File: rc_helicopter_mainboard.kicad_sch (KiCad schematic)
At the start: 15 parts, among them J1 Conn_01x06, SW1 Tactswitch, U1 STM32L4P5RET6, Y1 16MHz

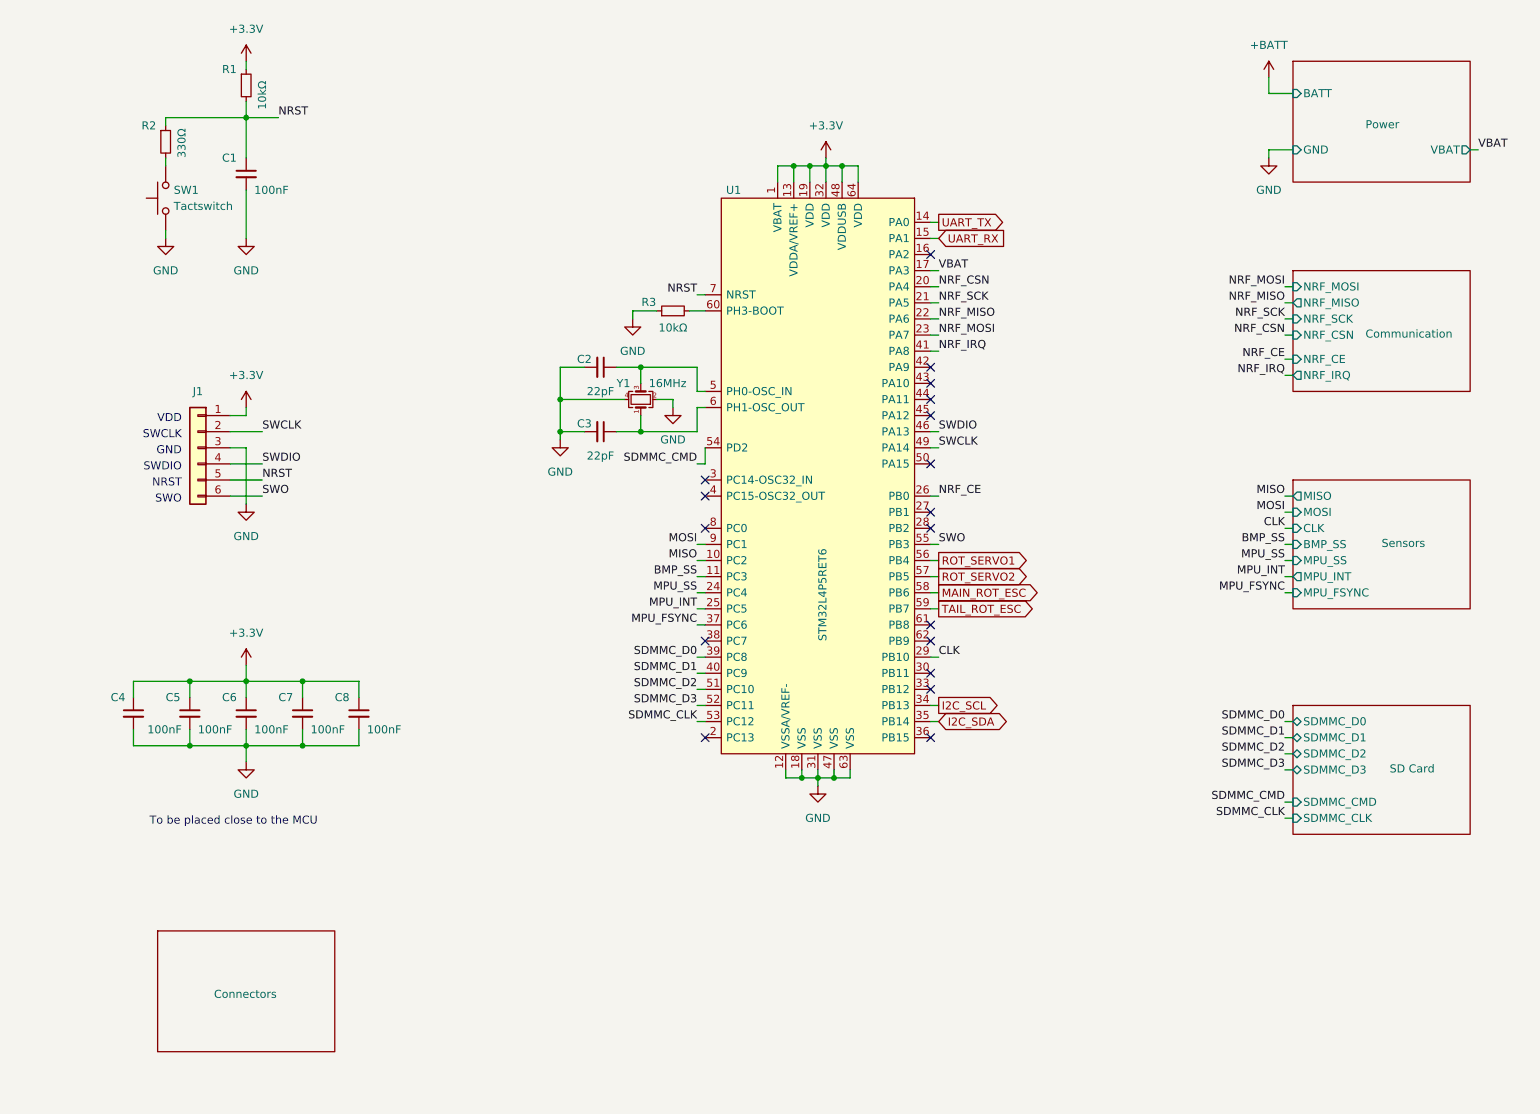
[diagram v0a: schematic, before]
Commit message: Use single connector for I/O
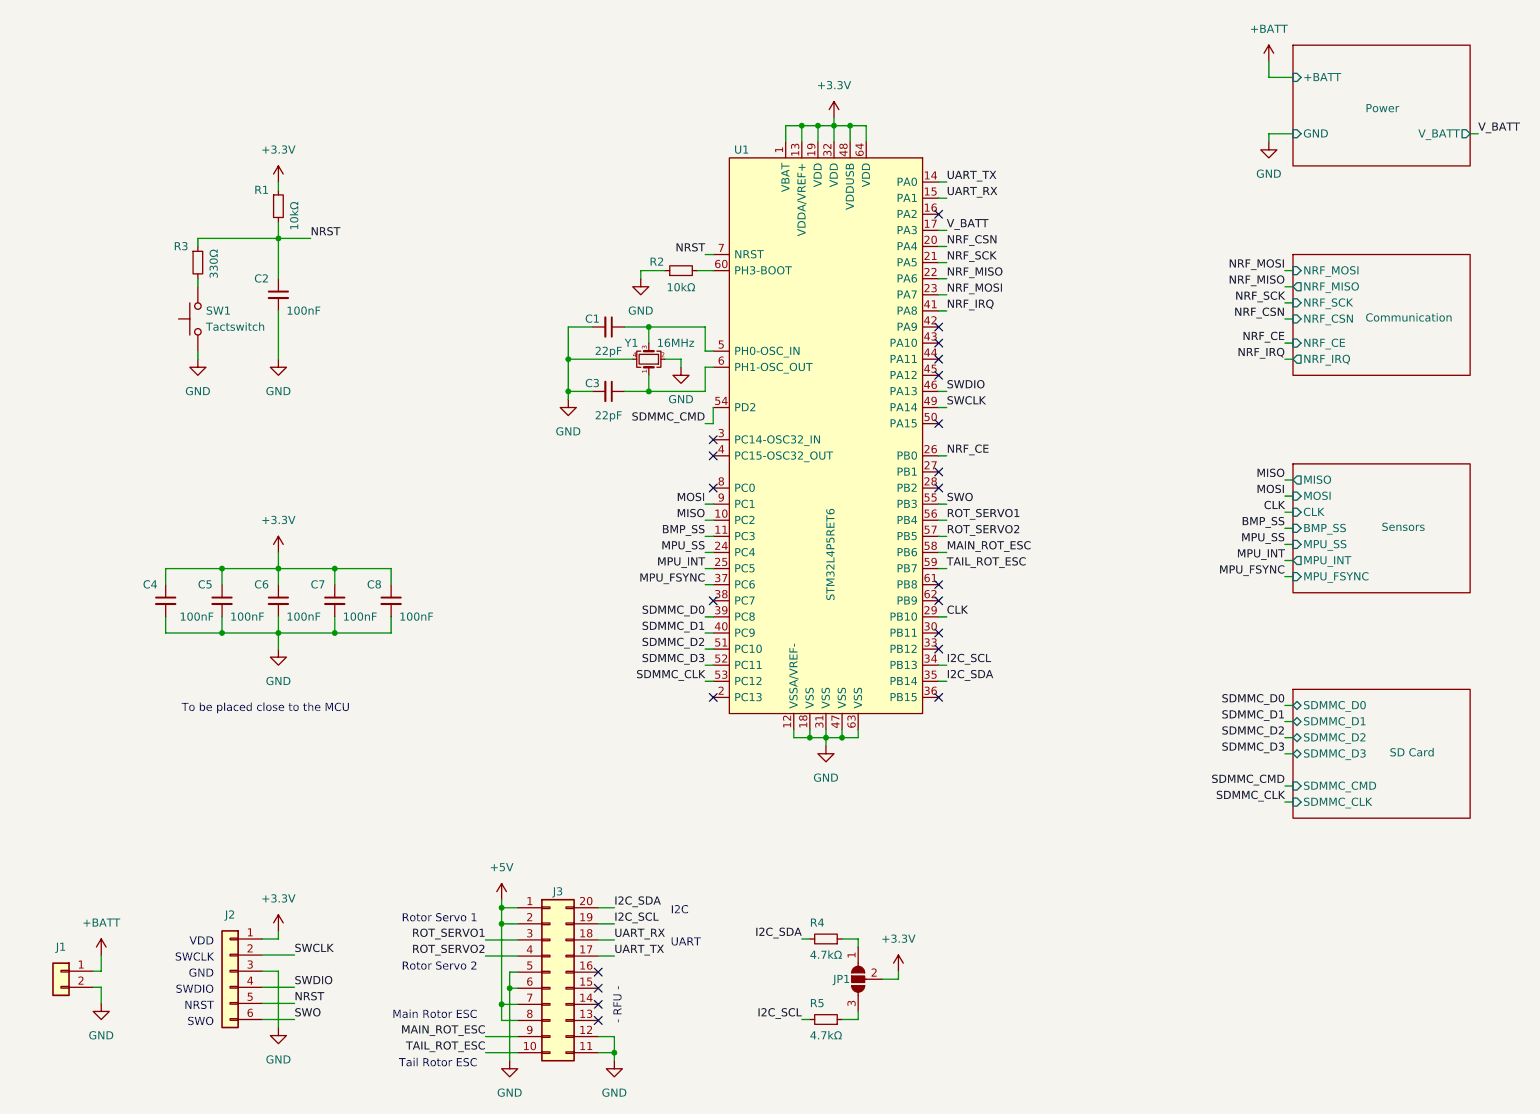
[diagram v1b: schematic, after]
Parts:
- added J1: Battery Pack, Connector_Molex:Molex_KK-254_AE-6410-02A_1x02_P2.54mm_Vertical, symbol Connector_Generic:Conn_01x02
- added J3: Main Connector, Connector_PinHeader_2.54mm:PinHeader_2x10_P2.54mm_Horizontal, symbol Connector_Generic:Conn_02x10_Counter_Clockwise
- added JP1: SolderJumper_3_Open, Jumper:SolderJumper-3_P1.3mm_Open_RoundedPad1.0x1.5mm_NumberLabels, symbol Jumper:SolderJumper_3_Open
- added R4, R5: 4.7kΩ, Resistor_SMD:R_0603_1608Metric, symbol Device:R_Small
- J2: renamed from J1; value Conn_01x06 -> SWD; footprint Connector_PinHeader_2.54mm:PinHeader_1x06_P2.54mm_Vertical_SMD_Pin1Left -> Connector_PinHeader_2.54mm:PinHeader_2x03_P2.54mm_Vertical
- renumbered C2 to C1, C1 to C2, R3 to R2, R2 to R3
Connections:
- net +3.3V: now also JP1.2 (C)
- net +BATT: now also J1.1 (Pin_1)
- net GND: now also J1.2 (Pin_2), J3.11 (Pin_11), J3.12 (Pin_12), J3.5 (Pin_5), J3.6 (Pin_6)
- net I2C_SCL: now also J3.19 (Pin_19), R5.2
- net I2C_SDA: now also J3.20 (Pin_20), R4.2
- net MAIN_ROT_ESC: now also J3.9 (Pin_9)
- net ROT_SERVO1: now also J3.3 (Pin_3)
- net ROT_SERVO2: now also J3.4 (Pin_4)
- net TAIL_ROT_ESC: now also J3.10 (Pin_10)
- net UART_RX: now also J3.18 (Pin_18)
- net UART_TX: now also J3.17 (Pin_17)
- net VBAT renamed V_BATT
- new net: JP1.1 (A), R4.1
- new net: JP1.3 (B), R5.1
- new net +5V: J3.1 (Pin_1), J3.2 (Pin_2), J3.7 (Pin_7), J3.8 (Pin_8)
- no-connect marks 18 -> 22
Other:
- removed sheet Connectors
- sheet Power ports: added +BATT, V_BATT; removed BATT, VBAT
- note added: "- RFU -"
- note added: "I2C"
- note added: "Main Rotor ESC"
- note added: "Rotor Servo 1"
- note added: "Rotor Servo 2"
- note added: "Tail Rotor ESC"
- note added: "UART"
- moved on the sheet: C1, C2, C3, C4, C5, C6, C7, C8, J2, R1, R2, R3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

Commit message: Remove 5V LDO regulator
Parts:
- renumbered C2 to C1, C1 to C2, R3 to R2, R2 to R3
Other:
- note added: "External I2C pull-ups"
- note added: "Main connector"
- note added: "Power in"
- note added: "SWD programmer"
- note added: "Short 1, 2 & 3 together for external I2C pull-ups"

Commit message: Arrange footprints
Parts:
- renumbered C2 to C1, C3 to C2, C1 to C3, R3 to R1, R1 to R2, R2 to R3
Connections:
- net LED1: now reaches U1.2 (PC13)
- net LED5: now reaches U1.27 (PB1)
- net LED2: now reaches U1.3 (PC14-OSC32_IN)
- net LED3: now reaches U1.4 (PC15-OSC32_OUT)
- net LED4: now reaches U1.8 (PC0)
- no-connect marks 22 -> 17
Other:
- added sheet LEDs (leds.kicad_sch)
- note added: "+"
- note added: "-"
- company: (none) -> Authors: H. Fedarovich, I. Kajdan
- moved on the sheet: C3, C4, C5, C6, C7, C8, R2, R3, SW1

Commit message: Move symbols to a separate directory
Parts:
- U1: symbol Local_Library:STM32L4P5RET6 -> STM32L4P5RET6:STM32L4P5RET6
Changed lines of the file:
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@@
     (pin "1")
   )
-  (symbol (lib_id "Local_Library:STM32L4P5RET6") (at 149.86 87.63 0) (unit 1)
+  (symbol (lib_id "STM32L4P5RET6:STM32L4P5RET6") (at 149.86 87.63 0) (unit 1)
     (in_bom yes) (on_board yes)
     (property "Reference" "U1" (id 0) (at 135.3694 44.45 0)
@@
     )
     (path "/8027772a-0953-4782-8447-2c100ffa6fed/009a44ff-8637-4954-850b-258100f52c64"
-      (reference "#PWR?") (unit 1) (value "GND") (footprint "")
+      (reference "#PWR0101") (unit 1) (value "GND") (footprint "")
     )
     (path "/7fcb5845-981d-459f-a7b6-0448545fef62"

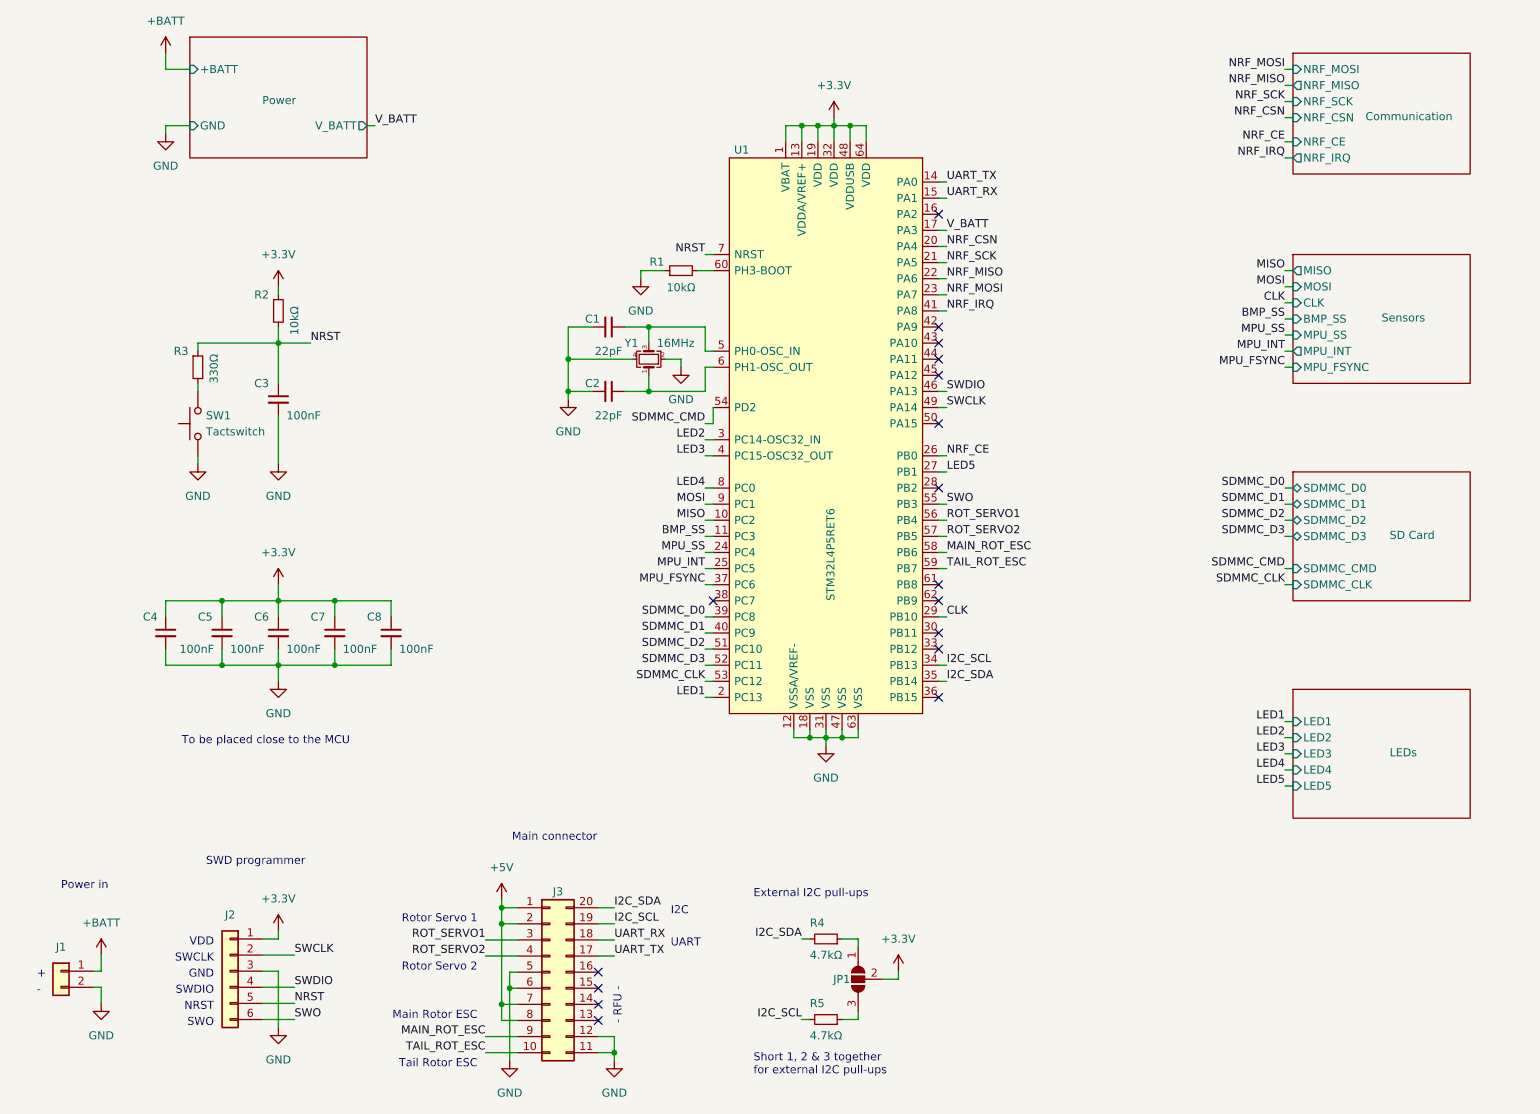
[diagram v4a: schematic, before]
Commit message: Rearrange footprints
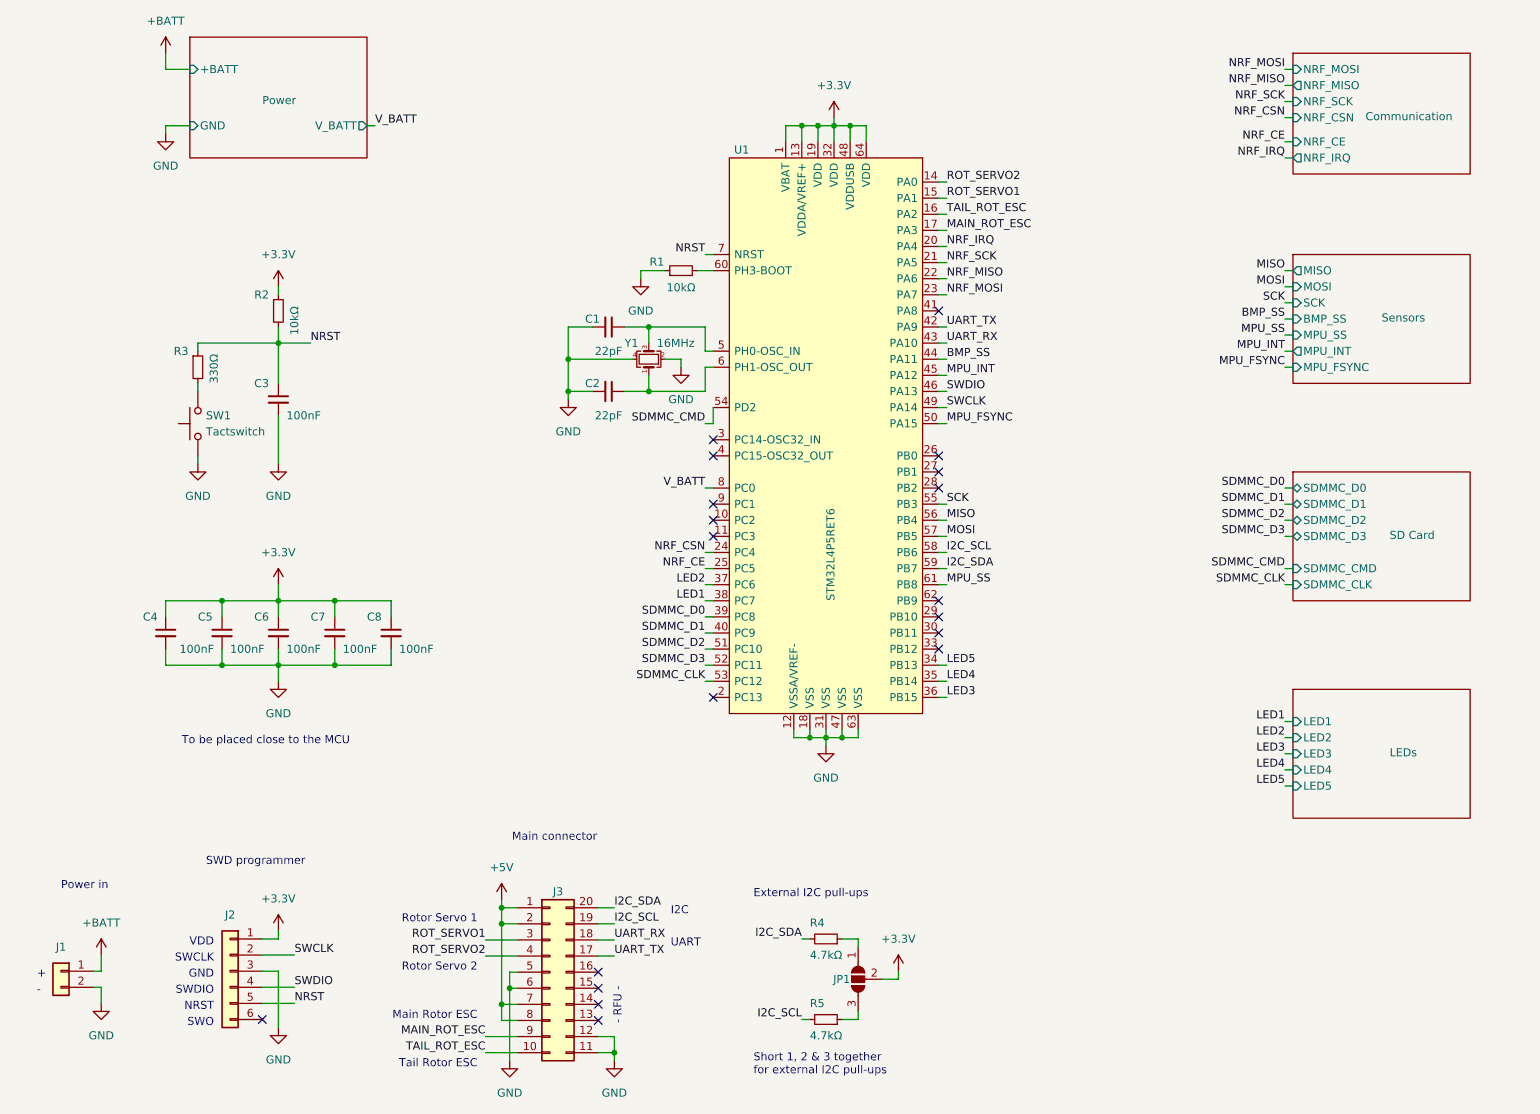
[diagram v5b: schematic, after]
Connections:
- net BMP_SS: now also U1.44 (PA11); no longer U1.11 (PC3)
- net I2C_SCL: now also U1.58 (PB6); no longer U1.34 (PB13)
- net I2C_SDA: now also U1.59 (PB7); no longer U1.35 (PB14)
- net LED1: now also U1.38 (PC7); no longer U1.2 (PC13)
- net LED2: now also U1.37 (PC6); no longer U1.3 (PC14-OSC32_IN)
- net LED3: now also U1.36 (PB15); no longer U1.4 (PC15-OSC32_OUT)
- net LED4: now also U1.35 (PB14); no longer U1.8 (PC0)
- net LED5: now also U1.34 (PB13); no longer U1.27 (PB1)
- net MAIN_ROT_ESC: now also U1.17 (PA3); no longer U1.58 (PB6)
- net MISO: now also U1.56 (PB4); no longer U1.10 (PC2)
- net MOSI: now also U1.57 (PB5); no longer U1.9 (PC1)
- net MPU_FSYNC: now also U1.50 (PA15); no longer U1.37 (PC6)
- net MPU_INT: now also U1.45 (PA12); no longer U1.25 (PC5)
- net MPU_SS: now also U1.61 (PB8); no longer U1.24 (PC4)
- net NRF_CE: now also U1.25 (PC5); no longer U1.26 (PB0)
- net NRF_CSN: now also U1.24 (PC4); no longer U1.20 (PA4)
- net NRF_IRQ: now also U1.20 (PA4); no longer U1.41 (PA8)
- net ROT_SERVO1: now also U1.15 (PA1); no longer U1.56 (PB4)
- net ROT_SERVO2: now also U1.14 (PA0); no longer U1.57 (PB5)
- net TAIL_ROT_ESC: now also U1.16 (PA2); no longer U1.59 (PB7)
- net UART_RX: now also U1.43 (PA10); no longer U1.15 (PA1)
- net UART_TX: now also U1.42 (PA9); no longer U1.14 (PA0)
- net V_BATT: now also U1.8 (PC0); no longer U1.17 (PA3)
- net CLK: no longer names the net of U1.29 (PB10)
- net SWO: no longer names the net of J2.6 (Pin_6)
- net SWO: no longer U1.55 (PB3)
- new net SCK: U1.55 (PB3)
- no-connect marks 17 -> 19
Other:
- sheet Sensors ports: added SCK; removed CLK
